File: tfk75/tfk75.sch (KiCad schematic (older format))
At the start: 13 parts, among them J1 USB_C_Receptacle, U1 MCP1700-3302E_SOT23, Y1 Resonator

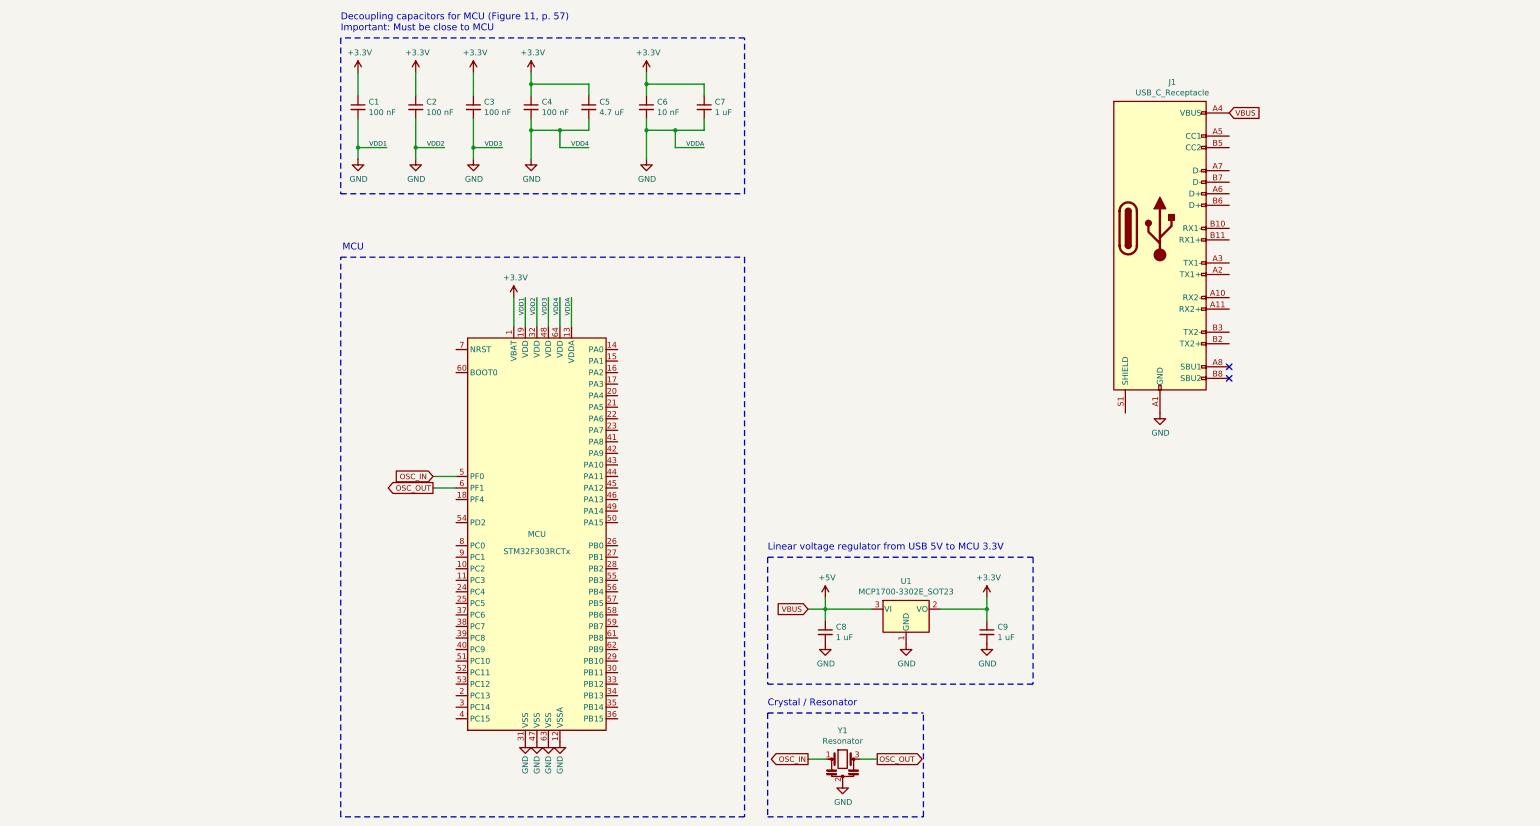
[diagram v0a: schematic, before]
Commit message: Add key matrix schematic
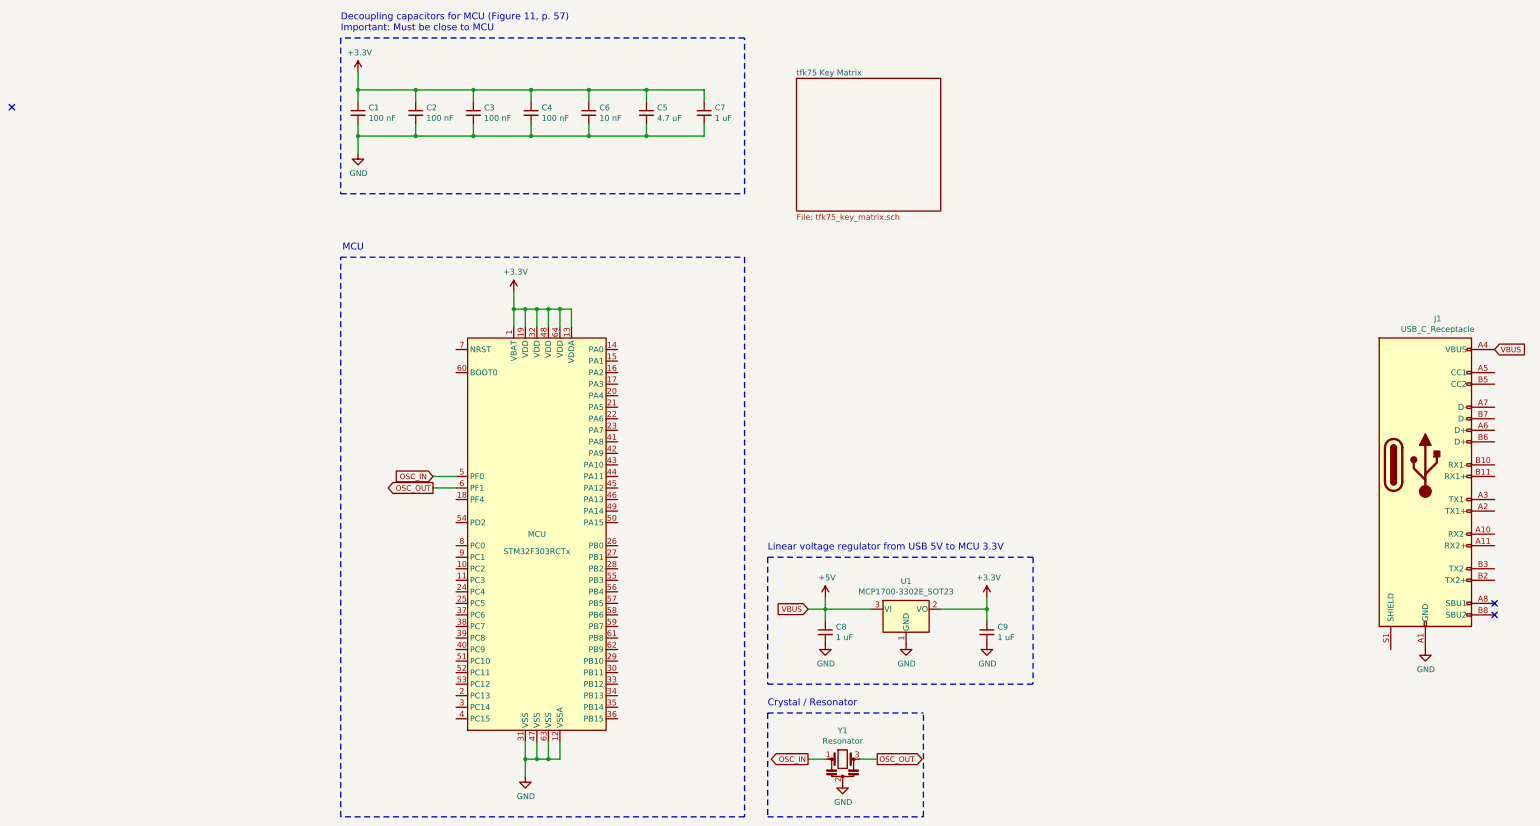
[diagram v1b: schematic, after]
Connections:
- net +3V3: now also MCU.13 (VDDA), MCU.19 (VDD), MCU.32 (VDD), MCU.48 (VDD), MCU.64 (VDD)
- net GND: no longer MCU.13 (VDDA), MCU.19 (VDD), MCU.32 (VDD), MCU.48 (VDD), MCU.64 (VDD)
- no-connect marks 2 -> 3
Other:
- moved on the sheet: C1, C2, C3, C4, C5, C6, C7, J1

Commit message: Begin key matrix
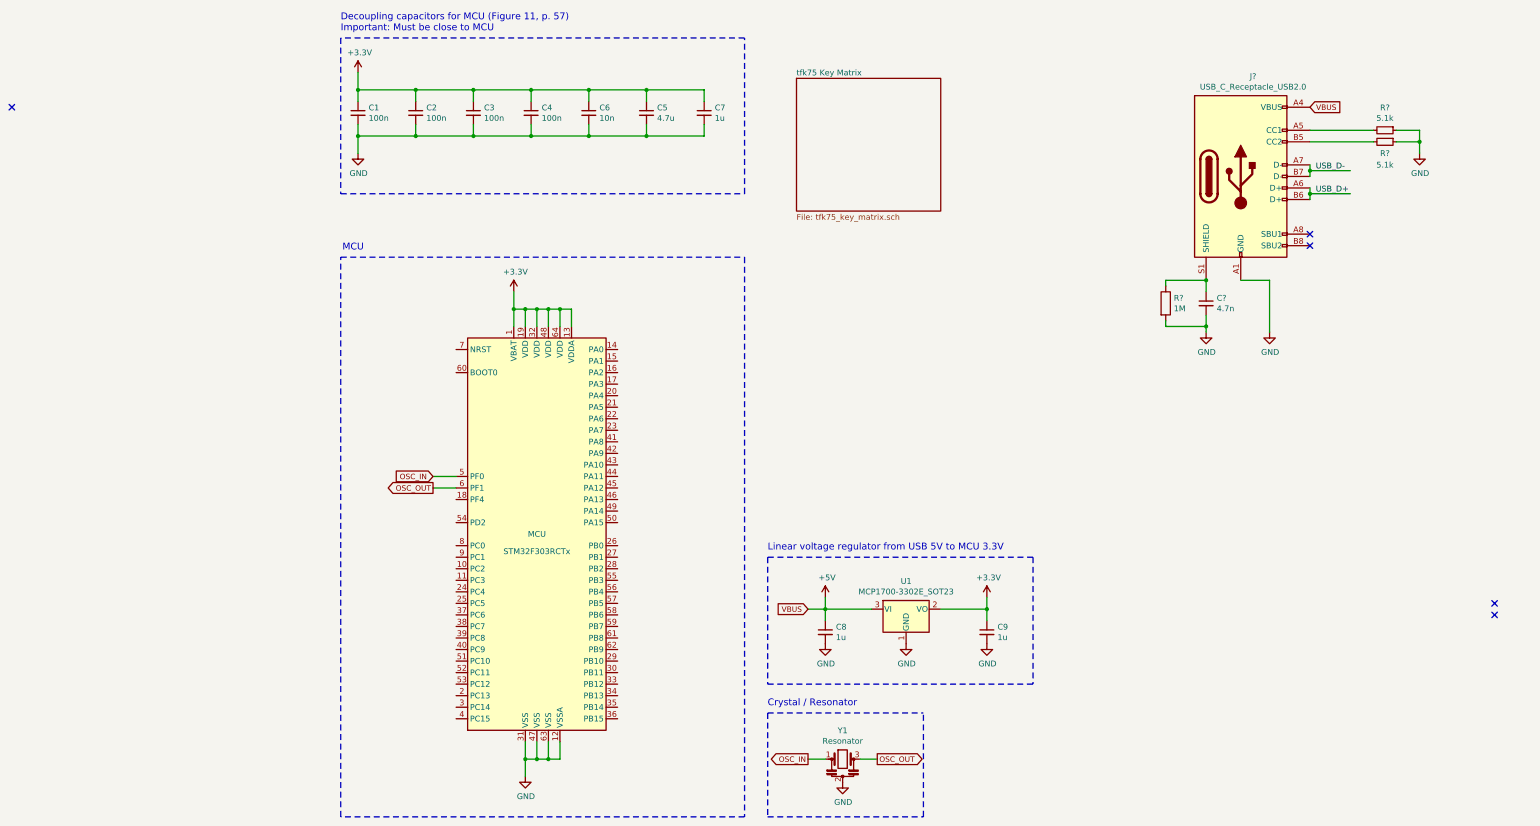
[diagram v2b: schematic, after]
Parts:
- removed J1: USB_C_Receptacle, symbol Connector:USB_C_Receptacle
- added C?: 4.7n, symbol Device:C_Small
- added J?: USB_C_Receptacle_USB2.0, symbol Connector:USB_C_Receptacle_USB2.0
- added R? (x2): 5.1k, symbol Device:R_Small
- added R?: 1M, symbol Device:R
- C1, C2, C3, C4: value 100 nF -> 100n
- C5: value 4.7 uF -> 4.7u
- C6: value 10 nF -> 10n
- C7, C8, C9: value 1 uF -> 1u
- MCU: Reference Manual (none) -> https://www.st.com/resource/en/reference_manual/dm00043574-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
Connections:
- net labels added: USB_D+, USB_D-
- wire segments 59 -> 80
- no-connect marks 3 -> 5
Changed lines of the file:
@@
 P 800 1500
 F 0 "C1" H 892 1546 50  0000 L CNN
-F 1 "100 nF" H 892 1455 50  0000 L CNN
+F 1 "100n" H 892 1455 50  0000 L CNN
 F 2 "" H 800 1500 50  0001 C CNN
 F 3 "~" H 800 1500 50  0001 C CNN
@@
 P 1800 1500
 F 0 "C3" H 1892 1546 50  0000 L CNN
-F 1 "100 nF" H 1892 1455 50  0000 L CNN
+F 1 "100n" H 1892 1455 50  0000 L CNN
 F 2 "" H 1800 1500 50  0001 C CNN
 F 3 "~" H 1800 1500 50  0001 C CNN
@@
 P 2300 1500
 F 0 "C4" H 2392 1546 50  0000 L CNN
-F 1 "100 nF" H 2392 1455 50  0000 L CNN
+F 1 "100n" H 2392 1455 50  0000 L CNN
 F 2 "" H 2300 1500 50  0001 C CNN
 F 3 "~" H 2300 1500 50  0001 C CNN
@@
 P 3300 1500
 F 0 "C5" H 3392 1546 50  0000 L CNN
-F 1 "4.7 uF" H 3392 1455 50  0000 L CNN
+F 1 "4.7u" H 3392 1455 50  0000 L CNN
 F 2 "" H 3300 1500 50  0001 C CNN
 F 3 "~" H 3300 1500 50  0001 C CNN
@@
 P 1300 1500
 F 0 "C2" H 1392 1546 50  0000 L CNN
-F 1 "100 nF" H 1392 1455 50  0000 L CNN
+F 1 "100n" H 1392 1455 50  0000 L CNN
 F 2 "" H 1300 1500 50  0001 C CNN
 F 3 "~" H 1300 1500 50  0001 C CNN
@@
 P 2800 1500
 F 0 "C6" H 2892 1546 50  0000 L CNN
-F 1 "10 nF" H 2892 1455 50  0000 L CNN
+F 1 "10n" H 2892 1455 50  0000 L CNN
 F 2 "" H 2800 1500 50  0001 C CNN
 F 3 "~" H 2800 1500 50  0001 C CNN
@@
 P 3800 1500
 F 0 "C7" H 3892 1546 50  0000 L CNN
-F 1 "1 uF" H 3892 1455 50  0000 L CNN
+F 1 "1u" H 3892 1455 50  0000 L CNN
 F 2 "" H 3800 1500 50  0001 C CNN
 F 3 "~" H 3800 1500 50  0001 C CNN
@@
 F 2 "Package_QFP:LQFP-64_10x10mm_P0.5mm" H 1750 3450 50  0001 R CNN
 F 3 "http://www.st.com/st-web-ui/static/active/en/resource/technical/document/datasheet/DM00058181.pdf" H 2750 2100 50  0001 C CNN
+F 4 "https://www.st.com/resource/en/reference_manual/dm00043574-stm32f303xbcde-stm32f303x68-stm32f328x8-stm32f358xc-stm32f398xe-advanced-armbased-mcus-stmicroelectronics.pdf" H 2350 5150 50  0001 C CNN "Reference Manual"
 	1    2350 5150
 	1    0    0    -1
@@
 P 4850 6000
 F 0 "C8" H 4942 6046 50  0000 L CNN
-F 1 "1 uF" H 4942 5955 50  0000 L CNN
+F 1 "1u" H 4942 5955 50  0000 L CNN
 F 2 "" H 4850 6000 50  0001 C CNN
 F 3 "~" H 4850 6000 50  0001 C CNN
@@
 P 6250 6000
 F 0 "C9" H 6342 6046 50  0000 L CNN
-F 1 "1 uF" H 6342 5955 50  0000 L CNN
+F 1 "1u" H 6342 5955 50  0000 L CNN
 F 2 "" H 6250 6000 50  0001 C CNN
 F 3 "~" H 6250 6000 50  0001 C CNN
@@
 Text Notes 4350 5300 0    59   ~ 0
 Linear voltage regulator from USB 5V to MCU 3.3V
-$Comp
-L Connector:USB_C_Receptacle J1
-U 1 1 6011DF29
-P 10050 4550
-F 0 "J1" H 10157 5817 50  0000 C CNN
-F 1 "USB_C_Receptacle" H 10157 5726 50  0000 C CNN
-F 2 "" H 10200 4550 50  0001 C CNN
-F 3 "https://www.usb.org/sites/default/files/documents/usb_type-c.zip" H 10200 4550 50  0001 C CNN
-	1    10050 4550
-	1    0    0    -1
-$EndComp
-Text GLabel 10650 3550 2    47   Input ~ 0
+Text GLabel 9050 1450 2    47   Input ~ 0
 VBUS
-$Comp
-L power:GND #PWR?
-U 1 1 6012551D
-P 10050 6150
-F 0 "#PWR?" H 10050 5900 50  0001 C CNN
-F 1 "GND" H 10055 5977 50  0000 C CNN
-F 2 "" H 10050 6150 50  0001 C CNN
-F 3 "" H 10050 6150 50  0001 C CNN
-	1    10050 6150
-	1    0    0    -1
-$EndComp
 NoConn ~ 10650 5850
 NoConn ~ 10650 5750
@@
 F1 "tfk75_key_matrix.sch" 50
 $EndSheet
+Wire Wire Line
+	9050 2050 9050 2000
+Connection ~ 9050 2000
+Wire Wire Line
+	9050 2000 9050 1950
+Wire Wire Line
+	9050 2150 9050 2200
+Connection ~ 9050 2200
+Wire Wire Line
+	9050 2200 9050 2250
+Text Label 9100 2000 0    50   ~ 0
+USB_D-
+Text Label 9100 2200 0    50   ~ 0
+USB_D+
+Wire Wire Line
+	9050 2000 9400 2000
+Wire Wire Line
+	9050 2200 9400 2200
+$Comp
+L Connector:USB_C_Receptacle_USB2.0 J?
+U 1 1 601413ED
+P 8450 2050
+F 0 "J?" H 8557 2917 50  0000 C CNN
+F 1 "USB_C_Receptacle_USB2.0" H 8557 2826 50  0000 C CNN
+F 2 "" H 8600 2050 50  0001 C CNN
+F 3 "https://www.usb.org/sites/default/files/documents/usb_type-c.zip" H 8600 2050 50  0001 C CNN
+	1    8450 2050
+	1    0    0    -1
+$EndComp
+NoConn ~ 9050 2550
+NoConn ~ 9050 2650
+$Comp
+L Device:R_Small R?
+U 1 1 60151F7D
+P 9700 1650
+F 0 "R?" V 9504 1650 50  0000 C CNN
+F 1 "5.1k" V 9595 1650 50  0000 C CNN
+F 2 "" H 9700 1650 50  0001 C CNN
+F 3 "~" H 9700 1650 50  0001 C CNN
+	1    9700 1650
+	0    1    1    0
+$EndComp
+$Comp
+L Device:R_Small R?
+U 1 1 60153BF0
+P 9700 1750
+F 0 "R?" V 9800 1750 50  0000 C CNN
+F 1 "5.1k" V 9900 1750 50  0000 C CNN
+F 2 "" H 9700 1750 50  0001 C CNN
+F 3 "~" H 9700 1750 50  0001 C CNN
+	1    9700 1750
+	0    1    1    0
+$EndComp
+Wire Wire Line
+	9800 1750 10000 1750
+Wire Wire Line
+	10000 1750 10000 1850
+$Comp
+L power:GND #PWR?
+U 1 1 60158D0A
+P 10000 1850
+F 0 "#PWR?" H 10000 1600 50  0001 C CNN
+F 1 "GND" H 10005 1677 50  0000 C CNN
+F 2 "" H 10000 1850 50  0001 C CNN
+F 3 "" H 10000 1850 50  0001 C CNN
+	1    10000 1850
+	1    0    0    -1
+$EndComp
+Wire Wire Line
+	10000 1650 10000 1750
+Connection ~ 10000 1750
+Wire Wire Line
+	9800 1650 10000 1650
+Wire Wire Line
+	9050 1650 9600 1650
+Wire Wire Line
+	9050 1750 9600 1750
+Wire Wire Line
+	8150 3250 8150 3350
+Wire Wire Line
+	8150 3350 7800 3350
+Wire Wire Line
+	7800 3350 7800 3300
+Wire Wire Line
+	7800 2950 7800 3000
+Wire Wire Line
+	8150 3050 8150 2950
+$Comp
+L power:GND #PWR?
+U 1 1 6019DA71
+P 8150 3400
+F 0 "#PWR?" H 8150 3150 50  0001 C CNN
+F 1 "GND" H 8155 3227 50  0000 C CNN
+F 2 "" H 8150 3400 50  0001 C CNN
+F 3 "" H 8150 3400 50  0001 C CNN
+	1    8150 3400
+	1    0    0    -1
+$EndComp
+Wire Wire Line
+	8150 3400 8150 3350
+Connection ~ 8150 3350
+Connection ~ 8150 2950
+Wire Wire Line
+	7800 2950 8150 2950
+$Comp
+L Device:C_Small C?
+U 1 1 60193496
+P 8150 3150
+F 0 "C?" H 8242 3196 50  0000 L CNN
+F 1 "4.7n" H 8242 3105 50  0000 L CNN
+F 2 "" H 8150 3150 50  0001 C CNN
+F 3 "~" H 8150 3150 50  0001 C CNN
+	1    8150 3150
+	1    0    0    -1
+$EndComp
+$Comp
+L Device:R R?
+U 1 1 60192B79
+P 7800 3150
+F 0 "R?" H 7870 3196 50  0000 L CNN
+F 1 "1M" H 7870 3105 50  0000 L CNN
+F 2 "" V 7730 3150 50  0001 C CNN
+F 3 "~" H 7800 3150 50  0001 C CNN
+	1    7800 3150
+	1    0    0    -1
+$EndComp
+Wire Wire Line
+	8450 2950 8700 2950
+Wire Wire Line
+	8700 2950 8700 3400
+$Comp
+L power:GND #PWR?
+U 1 1 601AF22A
+P 8700 3400
+F 0 "#PWR?" H 8700 3150 50  0001 C CNN
+F 1 "GND" H 8705 3227 50  0000 C CNN
+F 2 "" H 8700 3400 50  0001 C CNN
+F 3 "" H 8700 3400 50  0001 C CNN
+	1    8700 3400
+	1    0    0    -1
+$EndComp
 $EndSCHEMATC

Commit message: Finish key matrix, start reset circuit
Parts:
- removed U1: MCP1700-3302E_SOT23, Package_TO_SOT_SMD:SOT-23, symbol Regulator_Linear:MCP1700-3302E_SOT23
- added C?: 0.1u, symbol Device:C_Small
- added D?: D_Small, symbol Device:D_Small
- added F?: 1A, symbol Device:Polyfuse_Small
- added Q?: DTC123J, symbol Transistor_BJT:DTC123J
- added SW?: SW_Push, symbol Switch:SW_Push
- added U?: LF33_TO252, Package_TO_SOT_SMD:TO-252-2, symbol Regulator_Linear:LF33_TO252
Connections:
- net labels added: BOOT0, COL_0, COL_1, COL_10, COL_11, COL_12, COL_13, COL_2, COL_3, COL_4, COL_5, COL_6, COL_7, COL_8, COL_9, I2C1_SCL, I2C1_SDA, I2C2_SCL, I2C2_SDA, NRST, ROW_0, ROW_1, ROW_2, ROW_3, ROW_4, ROW_5, ROW_6, SPI1_MISO, SPI1_MOSI, SPI1_SCK, SWCLK, SWDIO, SWO
- wire segments 80 -> 150
- no-connect marks 5 -> 19
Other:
- note added: "Key matrix"
- moved on the sheet: C8, C9, C?, J?, R?, Y1

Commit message: Begin RGB matrix
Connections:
- net RGB_MATRIX: now reaches MCU.14 (PA0)
- net COL_14: now reaches MCU.3 (PC14)
- no-connect marks 19 -> 17
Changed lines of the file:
@@
 Wire Wire Line
 	800  1150 800  1300
-$Sheet
-S 4850 1050 550  2300
-U 60121801
-F0 "tfk75 Key Matrix" 50
-F1 "tfk75_key_matrix.sch" 50
-F2 "COL_0" I L 4850 1150 50
-F3 "COL_1" I L 4850 1250 50
-F4 "COL_2" I L 4850 1350 50
-F5 "ROW_0" I L 4850 2650 50
-F6 "COL_3" I L 4850 1450 50
-F7 "COL_4" I L 4850 1550 50
-F8 "COL_5" I L 4850 1650 50
-F9 "COL_6" I L 4850 1750 50
-F10 "COL_7" I L 4850 1850 50
-F11 "COL_8" I L 4850 1950 50
-F12 "COL_9" I L 4850 2050 50
-F13 "COL_10" I L 4850 2150 50
-F14 "COL_11" I L 4850 2250 50
-F15 "COL_12" I L 4850 2350 50
-F16 "ROW_1" I L 4850 2750 50
-F17 "ROW_2" I L 4850 2850 50
-F18 "ROW_3" I L 4850 2950 50
-F19 "ROW_4" I L 4850 3050 50
-F20 "ROW_5" I L 4850 3150 50
-F21 "ROW_6" I L 4850 3250 50
-F22 "COL_13" I L 4850 2450 50
-$EndSheet
 Text Label 9500 4300 0    50   ~ 0
 USB_D-
@@
 	4850 2450 4750 2450
 Wire Wire Line
-	4850 2650 4750 2650
-Wire Wire Line
 	4850 2750 4750 2750
 Wire Wire Line
-	4750 2850 4850 2850
+	4850 2850 4750 2850
 Wire Wire Line
 	4750 2950 4850 2950
 Wire Wire Line
-	4850 3050 4750 3050
+	4750 3050 4850 3050
 Wire Wire Line
 	4850 3150 4750 3150
 Wire Wire Line
-	4750 3250 4850 3250
+	4850 3250 4750 3250
+Wire Wire Line
+	4750 3350 4850 3350
 Text Label 4750 1450 2    50   ~ 0
 COL_3
@@
 Text Label 4750 2450 2    50   ~ 0
 COL_13
-Text Label 4750 2650 2    50   ~ 0
+Text Label 4750 2750 2    50   ~ 0
 ROW_0
-Text Label 4750 2750 2    50   ~ 0
+Text Label 4750 2850 2    50   ~ 0
 ROW_1
-Text Label 4750 2850 2    50   ~ 0
+Text Label 4750 2950 2    50   ~ 0
 ROW_2
-Text Label 4750 2950 2    50   ~ 0
+Text Label 4750 3050 2    50   ~ 0
 ROW_3
-Text Label 4750 3050 2    50   ~ 0
+Text Label 4750 3150 2    50   ~ 0
 ROW_4
+Text Label 4750 3350 2    50   ~ 0
+ROW_6
 Text Label 4750 3250 2    50   ~ 0
-ROW_6
-Text Label 4750 3150 2    50   ~ 0
 ROW_5
 Wire Notes Line
@@
 COL_13
 NoConn ~ 1650 6750
-NoConn ~ 1650 6650
 Wire Wire Line
 	3050 6150 3150 6150
@@
 NoConn ~ 3050 3750
 NoConn ~ 3050 3650
-NoConn ~ 3050 3550
 NoConn ~ 1650 4850
 NoConn ~ 1650 5050
-$Sheet
-S 6300 900  600  1600
-U 60AB8722
-F0 "tfk75 RGB Matrix" 50
-F1 "tfk_rgb_matrix.sch" 50
-$EndSheet
 Wire Wire Line
 	8800 5300 8800 5700
@@
 Wire Wire Line
 	5250 4800 5600 4800
+Wire Wire Line
+	6750 1150 6850 1150
+Text Label 6750 1150 2    50   ~ 0
+RGB_MATRIX
+Wire Wire Line
+	3050 3550 3150 3550
+Text Label 3150 3550 0    50   ~ 0
+RGB_MATRIX
+$Sheet
+S 4850 1050 550  2400
+U 60121801
+F0 "tfk75 Key Matrix" 50
+F1 "tfk75_key_matrix.sch" 50
+F2 "COL_0" I L 4850 1150 50
+F3 "COL_1" I L 4850 1250 50
+F4 "COL_2" I L 4850 1350 50
+F5 "ROW_0" I L 4850 2750 50
+F6 "COL_3" I L 4850 1450 50
+F7 "COL_4" I L 4850 1550 50
+F8 "COL_5" I L 4850 1650 50
+F9 "COL_6" I L 4850 1750 50
+F10 "COL_7" I L 4850 1850 50
+F11 "COL_8" I L 4850 1950 50
+F12 "COL_9" I L 4850 2050 50
+F13 "COL_10" I L 4850 2150 50
+F14 "COL_11" I L 4850 2250 50
+F15 "COL_12" I L 4850 2350 50
+F16 "ROW_1" I L 4850 2850 50
+F17 "ROW_2" I L 4850 2950 50
+F18 "ROW_3" I L 4850 3050 50
+F19 "ROW_4" I L 4850 3150 50
+F20 "ROW_5" I L 4850 3250 50
+F21 "ROW_6" I L 4850 3350 50
+F22 "COL_13" I L 4850 2450 50
+F23 "COL_14" I L 4850 2550 50
+$EndSheet
+Wire Wire Line
+	4750 2550 4850 2550
+Text Label 4750 2550 2    50   ~ 0
+COL_14
+Text Label 1550 6650 2    50   ~ 0
+COL_14
+Wire Wire Line
+	1550 6650 1650 6650
+$Sheet
+S 6850 1050 600  200
+U 60AB8722
+F0 "tfk75 RGB Matrix" 50
+F1 "tfk_rgb_matrix.sch" 50
+F2 "RGB_MATRIX" I L 6850 1150 50
+$EndSheet
 $EndSCHEMATC
